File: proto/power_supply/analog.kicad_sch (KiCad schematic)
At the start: 28 parts, among them U401 TSV914, U402 TSV914

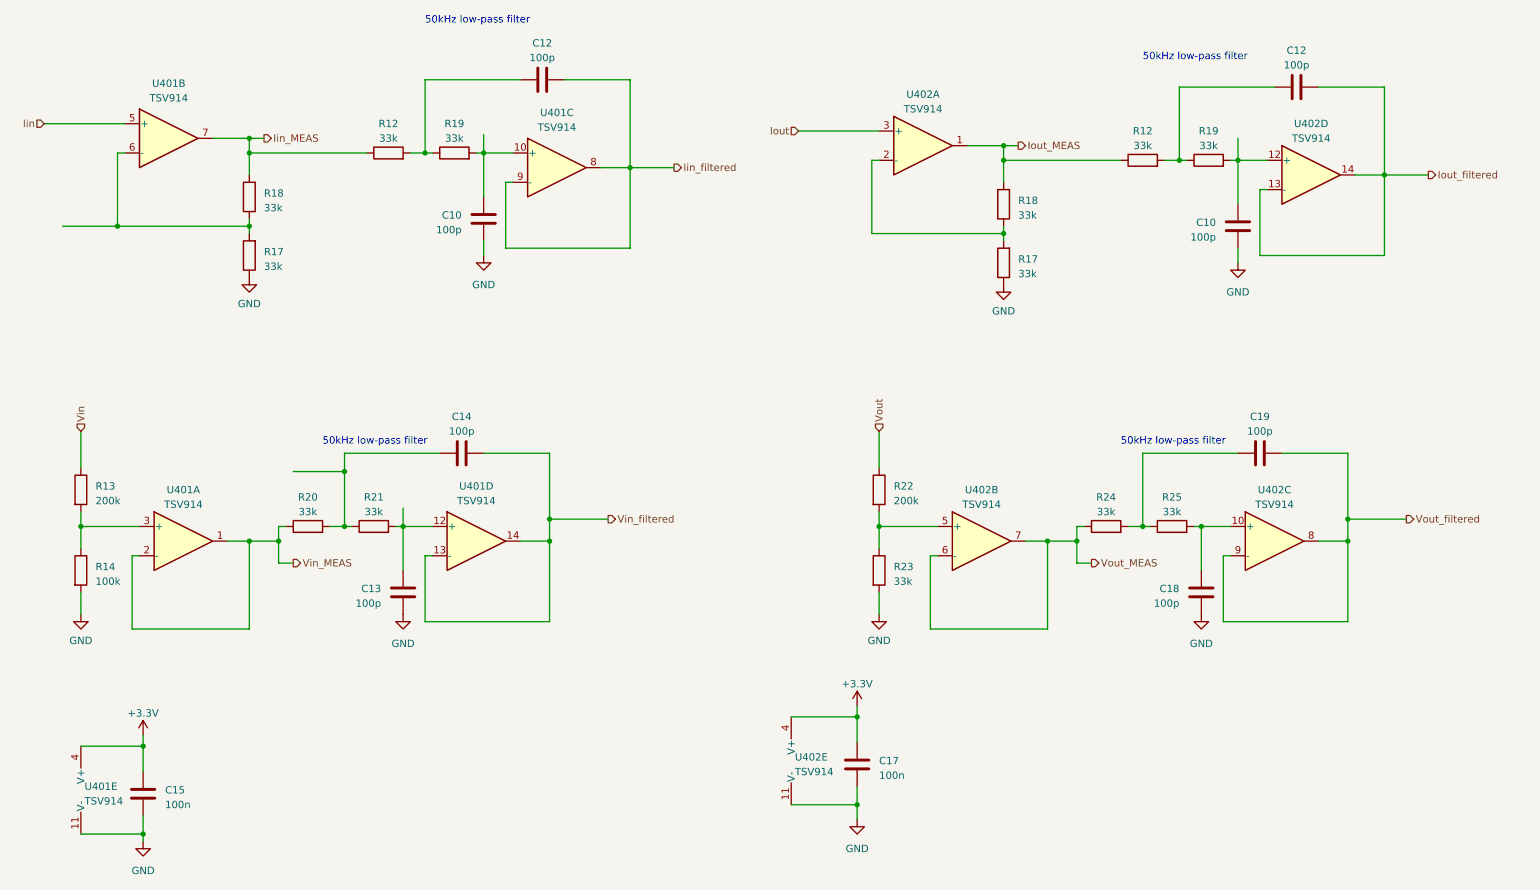
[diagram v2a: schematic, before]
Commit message: Update for BOM
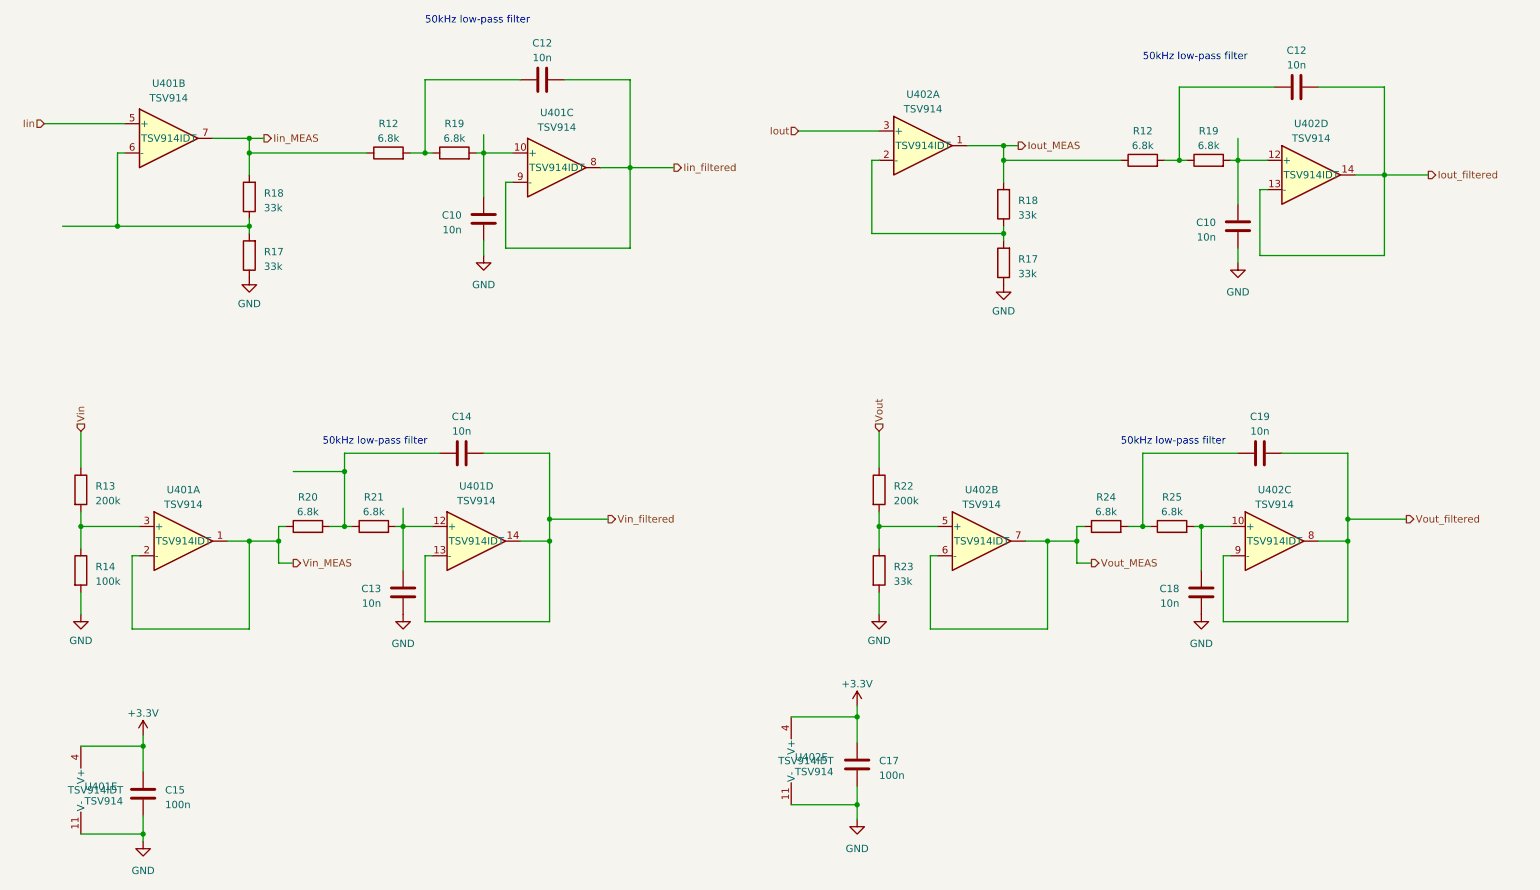
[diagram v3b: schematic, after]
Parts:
- C10, C12, C13, C14, C18, C19: value 100p -> 10n
- R12, R19, R20, R21, R24, R25: value 33k -> 6.8k
- U401, U402: MPN (none) -> TSV914IDT
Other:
- company: (none) -> Julien FAUCHER
- title: (none) -> MMPT PSU - Analog filtering
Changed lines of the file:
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@@
 (kicad_sch (version 20230221) (generator eeschema)
   (paper "A4")
+  (title_block
+    (title "MMPT PSU - Analog filtering")
+    (date "2023-04-05")
+    (rev "Rev. 1.0")
+    (company "Julien FAUCHER")
+    (comment 1 "Defis solaires 2023")
+  )
   (junction (at 257.81 50.8) (diameter 0) (color 0 0 0 0)
   )
@@
     (property "Datasheet" "www.st.com/resource/en/datasheet/tsv911.pdf" (at 50.8 109.22 0)
       (effects (font (size 1.27 1.27)) hide)
+    )
+    (property "MPN" "TSV914IDT" (at 49.53 114.3 0)
+      (effects (font (size 1.27 1.27)))
     )
     (pin "1")
@@
       (effects (font (size 1.27 1.27)) hide)
     )
+    (property "MPN" "TSV914IDT" (at 100.33 114.3 0)
+      (effects (font (size 1.27 1.27)))
+    )
     (pin "1")
     (pin "2")
@@
       (effects (font (size 1.27 1.27)) hide)
     )
+    (property "MPN" "TSV914IDT" (at 187.96 114.3 0)
+      (effects (font (size 1.27 1.27)))
+    )
     (pin "1")
     (pin "2")
@@
       (effects (font (size 1.27 1.27)))
     )
-    (property "Value" "100p" (at 236.22 95.25 90)
+    (property "Value" "10n" (at 236.22 95.25 90)
       (effects (font (size 1.27 1.27)))
     )
@@
       (effects (font (size 1.27 1.27)) (justify right))
     )
-    (property "Value" "100p" (at 83.82 125.095 0)
+    (property "Value" "10n" (at 83.82 125.095 0)
       (effects (font (size 1.27 1.27)) (justify right))
     )
@@
       (effects (font (size 1.27 1.27)))
     )
-    (property "Value" "33k" (at 215.9 45.72 90)
+    (property "Value" "6.8k" (at 215.9 45.72 90)
       (effects (font (size 1.27 1.27)))
     )
@@
       (effects (font (size 1.27 1.27)))
     )
-    (property "Value" "33k" (at 220.98 109.22 90)
+    (property "Value" "6.8k" (at 220.98 109.22 90)
       (effects (font (size 1.27 1.27)))
     )
@@
     (property "Datasheet" "www.st.com/resource/en/datasheet/tsv911.pdf" (at 48.26 39.37 0)
       (effects (font (size 1.27 1.27)) hide)
+    )
+    (property "MPN" "TSV914IDT" (at 46.99 44.45 0)
+      (effects (font (size 1.27 1.27)))
     )
     (pin "1")
@@
       (effects (font (size 1.27 1.27)))
     )
-    (property "Value" "100p" (at 111.76 30.48 90)
+    (property "Value" "10n" (at 111.76 30.48 90)
       (effects (font (size 1.27 1.27)))
     )
@@
     (property "Datasheet" "www.st.com/resource/en/datasheet/tsv911.pdf" (at 158.75 147.32 0)
       (effects (font (size 1.27 1.27)) hide)
+    )
+    (property "MPN" "TSV914IDT" (at 157.48 152.4 0)
+      (effects (font (size 1.27 1.27)))
     )
     (pin "1")
@@
       (effects (font (size 1.27 1.27)))
     )
-    (property "Value" "100p" (at 242.57 31.75 90)
+    (property "Value" "10n" (at 242.57 31.75 90)
       (effects (font (size 1.27 1.27)))
     )
@@
       (effects (font (size 1.27 1.27)))
     )
-    (property "Value" "33k" (at 82.55 109.22 90)
+    (property "Value" "6.8k" (at 82.55 109.22 90)
       (effects (font (size 1.27 1.27)))
     )
@@
       (effects (font (size 1.27 1.27)))
     )
-    (property "Value" "33k" (at 71.12 109.22 90)
+    (property "Value" "6.8k" (at 71.12 109.22 90)
       (effects (font (size 1.27 1.27)))
     )
@@
     (property "Datasheet" "www.st.com/resource/en/datasheet/tsv911.pdf" (at 35.56 152.4 0)
       (effects (font (size 1.27 1.27)) hide)
+    )
+    (property "MPN" "TSV914IDT" (at 34.29 157.48 0)
+      (effects (font (size 1.27 1.27)))
     )
     (pin "1")
@@
       (effects (font (size 1.27 1.27)) hide)
     )
+    (property "MPN" "TSV914IDT" (at 177.8 45.72 0)
+      (effects (font (size 1.27 1.27)))
+    )
     (pin "1")
     (pin "2")
@@
       (effects (font (size 1.27 1.27)) (justify right))
     )
-    (property "Value" "100p" (at 228.6 61.595 0)
+    (property "Value" "10n" (at 228.6 61.595 0)
       (effects (font (size 1.27 1.27)) (justify right))
     )
@@
       (effects (font (size 1.27 1.27)))
     )
-    (property "Value" "100p" (at 97.79 95.25 90)
+    (property "Value" "10n" (at 97.79 95.25 90)
       (effects (font (size 1.27 1.27)))
     )
@@
     (property "Datasheet" "www.st.com/resource/en/datasheet/tsv911.pdf" (at 240.03 109.22 0)
       (effects (font (size 1.27 1.27)) hide)
+    )
+    (property "MPN" "TSV914IDT" (at 238.76 114.3 0)
+      (effects (font (size 1.27 1.27)))
     )
     (pin "1")
@@
       (effects (font (size 1.27 1.27)) (justify right))
     )
-    (property "Value" "100p" (at 222.25 125.095 0)
+    (property "Value" "10n" (at 222.25 125.095 0)
       (effects (font (size 1.27 1.27)) (justify right))
     )
@@
       (effects (font (size 1.27 1.27)))
     )
-    (property "Value" "33k" (at 209.55 109.22 90)
+    (property "Value" "6.8k" (at 209.55 109.22 90)
       (effects (font (size 1.27 1.27)))
     )
@@
     (property "Datasheet" "www.st.com/resource/en/datasheet/tsv911.pdf" (at 115.57 44.45 0)
       (effects (font (size 1.27 1.27)) hide)
+    )
+    (property "MPN" "TSV914IDT" (at 114.3 49.53 0)
+      (effects (font (size 1.27 1.27)))
     )
     (pin "1")
@@
       (effects (font (size 1.27 1.27)) (justify right))
     )
-    (property "Value" "100p" (at 97.79 60.325 0)
+    (property "Value" "10n" (at 97.79 60.325 0)
       (effects (font (size 1.27 1.27)) (justify right))
     )
@@
     (property "Datasheet" "www.st.com/resource/en/datasheet/tsv911.pdf" (at 246.38 45.72 0)
       (effects (font (size 1.27 1.27)) hide)
+    )
+    (property "MPN" "TSV914IDT" (at 245.11 50.8 0)
+      (effects (font (size 1.27 1.27)))
     )
     (pin "1")
@@
       (effects (font (size 1.27 1.27)))
     )
-    (property "Value" "33k" (at 96.52 44.45 90)
+    (property "Value" "6.8k" (at 96.52 44.45 90)
       (effects (font (size 1.27 1.27)))
     )
@@
       (effects (font (size 1.27 1.27)))
     )
-    (property "Value" "33k" (at 227.33 45.72 90)
+    (property "Value" "6.8k" (at 227.33 45.72 90)
       (effects (font (size 1.27 1.27)))
     )
@@
       (effects (font (size 1.27 1.27)))
     )
-    (property "Value" "33k" (at 85.09 44.45 90)
-      (effects (font (size 1.27 1.27)))
-    )
+    (property "Value" "6.8k" (at 85.09 44.45 90)
+      (effects (font (size 1.27 1.27)))
+    )

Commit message: [PCB] Elaborate BOM
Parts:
- C15, C17: MPN (none) -> 0805YC104M4T2A; Mouser SKU (none) -> 581-0805YC104M4T2A
- U401, U402: Mouser SKU (none) -> 511-TSV914IDT

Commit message: Start overall new board
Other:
- note added: "Max for 3.3V is 23.3V"
- note added: "Max for 3.3V is 9.9V"
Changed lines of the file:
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@@
-(kicad_sch (version 20230221) (generator eeschema)
+(kicad_sch (version 20230409) (generator eeschema)
   (paper "A4")
   (title_block
@@
     (stroke (width 0) (type default))
   )
-  (text "50kHz low-pass filter" (at 73.66 97.79 0)
+  (text "Max for 3.3V is 23.3V" (exclude_from_sim no)
+ (at 168.91 86.36 0)
     (effects (font (size 1.27 1.27)) (justify left bottom))
   )
-  (text "50kHz low-pass filter" (at 215.9 31.115 0)
+  (text "50kHz low-pass filter" (exclude_from_sim no)
+ (at 73.66 97.79 0)
     (effects (font (size 1.27 1.27)) (justify left bottom))
   )
-  (text "50kHz low-pass filter" (at 91.44 24.765 0)
+  (text "50kHz low-pass filter" (exclude_from_sim no)
+ (at 215.9 31.115 0)
     (effects (font (size 1.27 1.27)) (justify left bottom))
   )
-  (text "50kHz low-pass filter" (at 212.09 97.79 0)
+  (text "50kHz low-pass filter" (exclude_from_sim no)
+ (at 91.44 24.765 0)
     (effects (font (size 1.27 1.27)) (justify left bottom))
   )
+  (text "50kHz low-pass filter" (exclude_from_sim no)
+ (at 212.09 97.79 0)
+    (effects (font (size 1.27 1.27)) (justify left bottom))
+  )
+  (text "Max for 3.3V is 9.9V" (exclude_from_sim no)
+ (at 33.02 87.63 0)
+    (effects (font (size 1.27 1.27)) (justify left bottom))
+  )
